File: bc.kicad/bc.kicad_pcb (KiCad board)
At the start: 2 copper layers, 90 x 50 mm, 21 parts, among them J1 Pin_Header_01x33_Male, J2 Capacitive Keyboard

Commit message: Experiment with keyboard backlighting
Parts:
- moved D5 3.88 mm to (119.3, 142.8), turned to 90 degrees
- moved D8 3.86 mm to (137.3, 142.8), turned to 90 degrees
- moved D7 3.83 mm to (131.4, 142.9), turned to 90 degrees
- moved D6 3.78 mm to (125.2, 142.8), turned to 90 degrees
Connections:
- J2 pad 1: (no net) -> /CAP_C1
- J2 pad 10: (no net) -> /CAP_A1
- J2 pad 11: (no net) -> /CAP_A#1
- J2 pad 12: (no net) -> /CAP_B1
- J2 pad 13: (no net) -> /CAP_C2
- J2 pad 2: (no net) -> /CAP_C#1
- J2 pad 3: (no net) -> /CAP_D1
- J2 pad 4: (no net) -> /CAP_D#1
- J2 pad 5: (no net) -> /CAP_E1
- J2 pad 6: (no net) -> /CAP_F1
- J2 pad 7: (no net) -> /CAP_F#1
- J2 pad 8: (no net) -> /CAP_G1
- J2 pad 9: (no net) -> /CAP_G#1
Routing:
- net /LED_GND: track 0.00 -> 176.5 mm, vias 0 -> 11
- net /LED_A1_B: track 0.00 -> 56.9 mm
- net /LED_C2_B: track 0.00 -> 54.0 mm
- net /LED_B1_B: track 0.00 -> 48.1 mm
- net /CAP_C1: track 0.00 -> 30.6 mm, vias 0 -> 1
- net /CAP_C#1: track 0.00 -> 30.1 mm, vias 0 -> 1
- net /CAP_D1: track 0.00 -> 29.3 mm, vias 0 -> 1
- net /CAP_D#1: track 0.00 -> 29.0 mm, vias 0 -> 1
- net /CAP_C2: track 0.00 -> 29.0 mm, vias 0 -> 1
- net /CAP_G1: track 0.00 -> 26.6 mm, vias 0 -> 1
- net /CAP_A1: track 0.00 -> 26.4 mm, vias 0 -> 1
- net /CAP_G#1: track 0.00 -> 26.3 mm, vias 0 -> 1
- net /CAP_F#1: track 0.00 -> 26.2 mm, vias 0 -> 1
- net /CAP_F1: track 0.00 -> 25.7 mm, vias 0 -> 1
- net /CAP_E1: track 0.00 -> 25.5 mm, vias 0 -> 1
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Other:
- board text added: "JLCJLCJLCJL"

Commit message: Layout keyboard half draft
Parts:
- removed J2: Capacitive Keyboard, bc:keyboard
- removed Ref**: Val**, bc:writing
- removed Ref**: Val**, bc:round_speaker_ring
- added BT1: CR2032, Battery:BatteryHolder_Keystone_3002_1x2032, B.Cu at (116.9, 60.6)
- added C1: 470nF, Capacitor_SMD:C_0402_1005Metric, B.Cu at (102.3, 72.1)
- added C10: 100nF, Capacitor_SMD:C_0402_1005Metric, B.Cu at (157.4, 61.5)
- added C11: 470nF, Capacitor_SMD:C_0402_1005Metric, B.Cu at (139.7, 65.6)
- added C12: 470nF, Capacitor_SMD:C_0402_1005Metric, B.Cu at (159.3, 61.6)
- added C13: 470nF, Capacitor_SMD:C_0402_1005Metric, B.Cu at (157.9, 68.9)
- added C14: 470nF, Capacitor_SMD:C_0402_1005Metric, B.Cu at (146.8, 55.5)
- added C15: 100nF, Capacitor_SMD:C_0402_1005Metric, B.Cu at (160.4, 52.3)
- added C16: 100nF, Capacitor_SMD:C_0402_1005Metric, B.Cu at (149.7, 69.3)
- added C17: 100nF, Capacitor_SMD:C_0402_1005Metric, B.Cu at (146.2, 69.5)
- added C18: 100nF, Capacitor_SMD:C_0402_1005Metric, B.Cu at (145.1, 68.0)
- added C19: 100nF, Capacitor_SMD:C_0402_1005Metric, B.Cu at (145.0, 58.4)
- added C2: 470nF, Capacitor_SMD:C_0402_1005Metric, B.Cu at (102.2, 70.8)
- added C20: 100nF, Capacitor_SMD:C_0402_1005Metric, B.Cu at (154.0, 57.3)
- added C21: Capacitive_Keyboard, bc:keyboard, F.Cu at (145.0, 75.0)
- added C3: 470nF, Capacitor_SMD:C_0402_1005Metric, B.Cu at (88.1, 73.5)
- added C4: 470nF, Capacitor_SMD:C_0402_1005Metric, B.Cu at (87.9, 75.1)
- added C5: 470nF, Capacitor_SMD:C_0402_1005Metric, B.Cu at (95.9, 67.6)
- added C6: 470nF, Capacitor_SMD:C_0402_1005Metric, B.Cu at (92.6, 67.7)
- added C7: 100nF, Capacitor_SMD:C_0402_1005Metric, B.Cu at (154.1, 68.9)
- added C8: 100nF, Capacitor_SMD:C_0402_1005Metric, B.Cu at (146.9, 56.7)
- added C9: 100nF, Capacitor_SMD:C_0402_1005Metric, B.Cu at (141.2, 65.6)
- added D17: LED_07A, bc:side_led, B.Cu at (173.7, 74.0)
- added D18: LED_03B, bc:side_led, B.Cu at (129.1, 97.0)
- added D19: LED_07B, bc:side_led, B.Cu at (171.5, 97.0)
- added D20: LED_11, bc:side_led, B.Cu at (143.4, 74.0)
- added D21: LED_04A, bc:side_led, B.Cu at (137.4, 74.0)
- added D22: LED_08A, bc:side_led, B.Cu at (181.8, 74.0)
- added D23: LED_04B, bc:side_led, B.Cu at (139.7, 97.0)
- added D24: LED_08B, bc:side_led, B.Cu at (182.0, 97.0)
- added D25: LED_12, bc:side_led, B.Cu at (155.5, 74.0)
- added D26: D_Schottky, Diode_SMD:D_SOD-123, B.Cu at (182.0, 36.0)
- added Q1: PMV48XP, Package_TO_SOT_SMD:SOT-23, B.Cu at (131.0, 55.0)
- added R1: 10K, Resistor_SMD:R_0402_1005Metric, B.Cu at (224.2, -15.0)
- added R10: 10K, Resistor_SMD:R_0402_1005Metric, B.Cu at (229.2, 20.0)
- added R11: 10K, Resistor_SMD:R_0402_1005Metric, B.Cu at (224.2, -10.0)
- added R12: 10K, Resistor_SMD:R_0402_1005Metric, B.Cu at (224.2, 19.0)
- added R13: 10K, Resistor_SMD:R_0402_1005Metric, B.Cu at (224.2, -5.00)
- added R14: 10K, Resistor_SMD:R_0402_1005Metric, B.Cu at (224.2, -20.0)
- added R15: 10K, Resistor_SMD:R_0402_1005Metric, B.Cu at (228.8, 1.00)
- added R16: 10K, Resistor_SMD:R_0402_1005Metric, B.Cu at (223.8, 1.00)
- added R2: 10K, Resistor_SMD:R_0402_1005Metric, B.Cu at (229.2, -5.00)
- added R3: 10K, Resistor_SMD:R_0402_1005Metric, B.Cu at (142.6, 52.6)
- added R4: 10K, Resistor_SMD:R_0402_1005Metric, B.Cu at (224.0, 26.0)
- added R5: 10K, Resistor_SMD:R_0402_1005Metric, B.Cu at (224.2, 13.0)
- added R6: 10K, Resistor_SMD:R_0402_1005Metric, B.Cu at (224.2, 7.00)
- added R7: 10K, Resistor_SMD:R_0402_1005Metric, B.Cu at (229.2, -11.0)
- added R8: 10K, Resistor_SMD:R_0402_1005Metric, B.Cu at (228.2, 13.0)
- added R9: 10K, Resistor_SMD:R_0402_1005Metric, B.Cu at (228.8, 7.00)
- added SW1: SW_Push, bc:SW_Push_1P1T_NO_5.1x5.1mm_H2.5mm, B.Cu at (167.1, 63.4)
- added TP1: Catch, bc:test_point, B.Cu at (102.0, 53.0)
- added TP2: Catch, bc:test_point, B.Cu at (102.0, 97.1)
- added TP3: Catch, bc:test_point, B.Cu at (135.7, 68.0)
- added TP4: Catch, bc:test_point, B.Cu at (188.0, 53.0)
- added TP5: Catch, bc:test_point, B.Cu at (188.0, 97.1)
- added U1: STM32L052C8Tx, Package_QFP:LQFP-48_7x7mm_P0.5mm, B.Cu at (149.7, 63.2)
- D1: value LED_C1 -> D_Schottky; footprint bc:side_led -> Diode_SMD:D_SOD-123
- D10: value LED_A1_T -> LED_13
- D11: value LED_A1_B -> LED_02A
- D12: value LED_A#1 -> LED_06A
- D13: value LED_B1_T -> LED_02B
- D14: value LED_B1_B -> LED_06B
- D15: value LED_C2_T -> LED_10
- D16: value LED_C2_B -> LED_03A
- D2: value LED_C#1 -> D_Schottky; footprint bc:side_led -> Diode_SMD:D_SOD-123
- D3: value LED_D1 -> D_Schottky; footprint bc:side_led -> Diode_SMD:D_SOD-123
- D4: value LED_D#1 -> D_Schottky; footprint bc:side_led -> Diode_SMD:D_SOD-123
- D5: value LED_E1 -> LED_01A
- D6: value LED_F1 -> LED_05A
- D7: value LED_F#1 -> LED_01B
- D8: value LED_G1 -> LED_05B
- D9: value LED_G#1 -> LED_09
- J1: value Pin_Header_01x33_Male -> Edge Connector; footprint Connector_PinHeader_2.54mm:PinHeader_1x33_P2.54mm_Vertical_SMD_Pin1Left -> bc:edge_connector
- LS1: value Speaker -> Transducer; footprint bc:wire_pad_3x5mm_x2 -> bc:transducer
- moved D1 148.4 mm to (202.3, 41.0), turned to 0 degrees
- moved D3 138.5 mm to (188.4, 30.0), turned to 0 degrees
- moved D4 138.3 mm to (199.3, 34.0), turned to 0 degrees
- moved D2 136.8 mm to (191.3, 40.0), turned to 0 degrees
- moved LS1 110.1 mm to (177.9, 63.2), turned to 180 degrees
- moved D16 98.7 mm to (131.1, 74.0), turned to 180 degrees
- moved D11 95.8 mm to (118.4, 74.0), turned to 180 degrees
- moved D15 79.7 mm to (124.8, 74.0)
- moved J1 75.7 mm to (163.0, 51.9), turned to 0 degrees
- moved D9 73.2 mm to (112.1, 74.0)
- moved D6 72.9 mm to (149.5, 74.0), turned to 180 degrees
- moved D5 70.2 mm to (105.9, 74.0), turned to 180 degrees
- moved D10 69.9 mm to (167.6, 74.0)
- moved D14 68.5 mm to (160.9, 97.0)
- moved D12 67.5 mm to (161.5, 74.0)
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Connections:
- D1 pad 1: /LED_GND -> Net-(C1-Pad2)
- D1 pad 2: /LED_C1 -> /LED_R0_PWR
- D10 pad 1: /LED_GND -> /LED_C0
- D10 pad 2: /LED_A1_T -> Net-(C6-Pad2)
- D11 pad 1: /LED_GND -> /LED_C1
- D11 pad 2: /LED_A1_B -> Net-(C1-Pad2)
- D12 pad 1: /LED_GND -> /LED_C1
- D12 pad 2: /LED_A#1 -> Net-(C3-Pad2)
- D13 pad 1: /LED_GND -> /LED_C1
- D13 pad 2: /LED_B1_T -> Net-(C1-Pad2)
- D14 pad 1: /LED_GND -> /LED_C1
- D14 pad 2: /LED_B1_B -> Net-(C3-Pad2)
- D15 pad 1: /LED_GND -> /LED_C1
- D15 pad 2: /LED_C2_T -> Net-(C5-Pad2)
- D16 pad 1: /LED_GND -> /LED_C2
- D16 pad 2: /LED_C2_B -> Net-(C1-Pad2)
- D2 pad 1: /LED_GND -> Net-(C3-Pad2)
- D2 pad 2: /LED_C#1 -> /LED_R1_PWR
- D3 pad 1: /LED_GND -> Net-(C5-Pad2)
- D3 pad 2: /LED_D1 -> /LED_R2_PWR
- D4 pad 1: /LED_GND -> Net-(C6-Pad2)
- D4 pad 2: /LED_D#1 -> /LED_R3_PWR
- D5 pad 1: /LED_GND -> /LED_C0
- D5 pad 2: /LED_E1 -> Net-(C1-Pad2)
- D6 pad 1: /LED_GND -> /LED_C0
- D6 pad 2: /LED_F1 -> Net-(C3-Pad2)
- D7 pad 1: /LED_GND -> /LED_C0
- D7 pad 2: /LED_F#1 -> Net-(C1-Pad2)
- D8 pad 1: /LED_GND -> /LED_C0
- D8 pad 2: /LED_G1 -> Net-(C3-Pad2)
- D9 pad 1: /LED_GND -> /LED_C0
- D9 pad 2: /LED_G#1 -> Net-(C5-Pad2)
- J1 pad 1: /SPEAKER+ -> GND
- J1 pad 2: /SPEAKER- -> /NRST
- J1 pad 3: /CAP_C1 -> /SWCLK
- J1 pad 4: /LED_C1 -> /SWDIO
- J1 pad 5: /CAP_C#1 -> /KEY_03_D1
- J1 pad 6: /LED_C#1 -> /KEY_02_C#1
- J1 pad 7: /CAP_D1 -> /BOOT0
- J1 pad 8: /LED_D1 -> VDD
- LS1 pad 1: /SPEAKER+ -> /TRANSDUCER
- LS1 pad 2: /SPEAKER- -> GND
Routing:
- net /LED_GND: track 176.5 -> 0.00 mm, vias 11 -> 0
- net Net-(C3-Pad2): track 0.00 -> 146.3 mm
- net Net-(C1-Pad2): track 0.00 -> 144.6 mm
- net /LED_C0: track 0.00 -> 70.3 mm
- net /LED_C3: track 0.00 -> 67.7 mm
- net /LED_C2: track 0.00 -> 57.6 mm
- net /LED_A1_B: track 56.9 -> 0.00 mm
- net /LED_C2_B: track 54.0 -> 0.00 mm
- net /LED_B1_B: track 48.1 -> 0.00 mm
- net /LED_C1: track 22.0 -> 67.3 mm
- net /CAP_C1: track 30.6 -> 0.00 mm, vias 1 -> 0
- net /CAP_C#1: track 30.1 -> 0.00 mm, vias 1 -> 0
- net /CAP_D1: track 29.3 -> 0.00 mm, vias 1 -> 0
- net /CAP_D#1: track 29.0 -> 0.00 mm, vias 1 -> 0
- net /CAP_C2: track 29.0 -> 0.00 mm, vias 1 -> 0
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- added copper zone on B.Cu, net GND
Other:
- outline, holes or cut-outs redrawn
- rule trace_min: 0.2 -> 0.15
- rule via_min_drill: 0.3 -> 0.2
- rule via_min_size: 0.4 -> 0.45
- board text removed: "JLCJLCJLCJL"

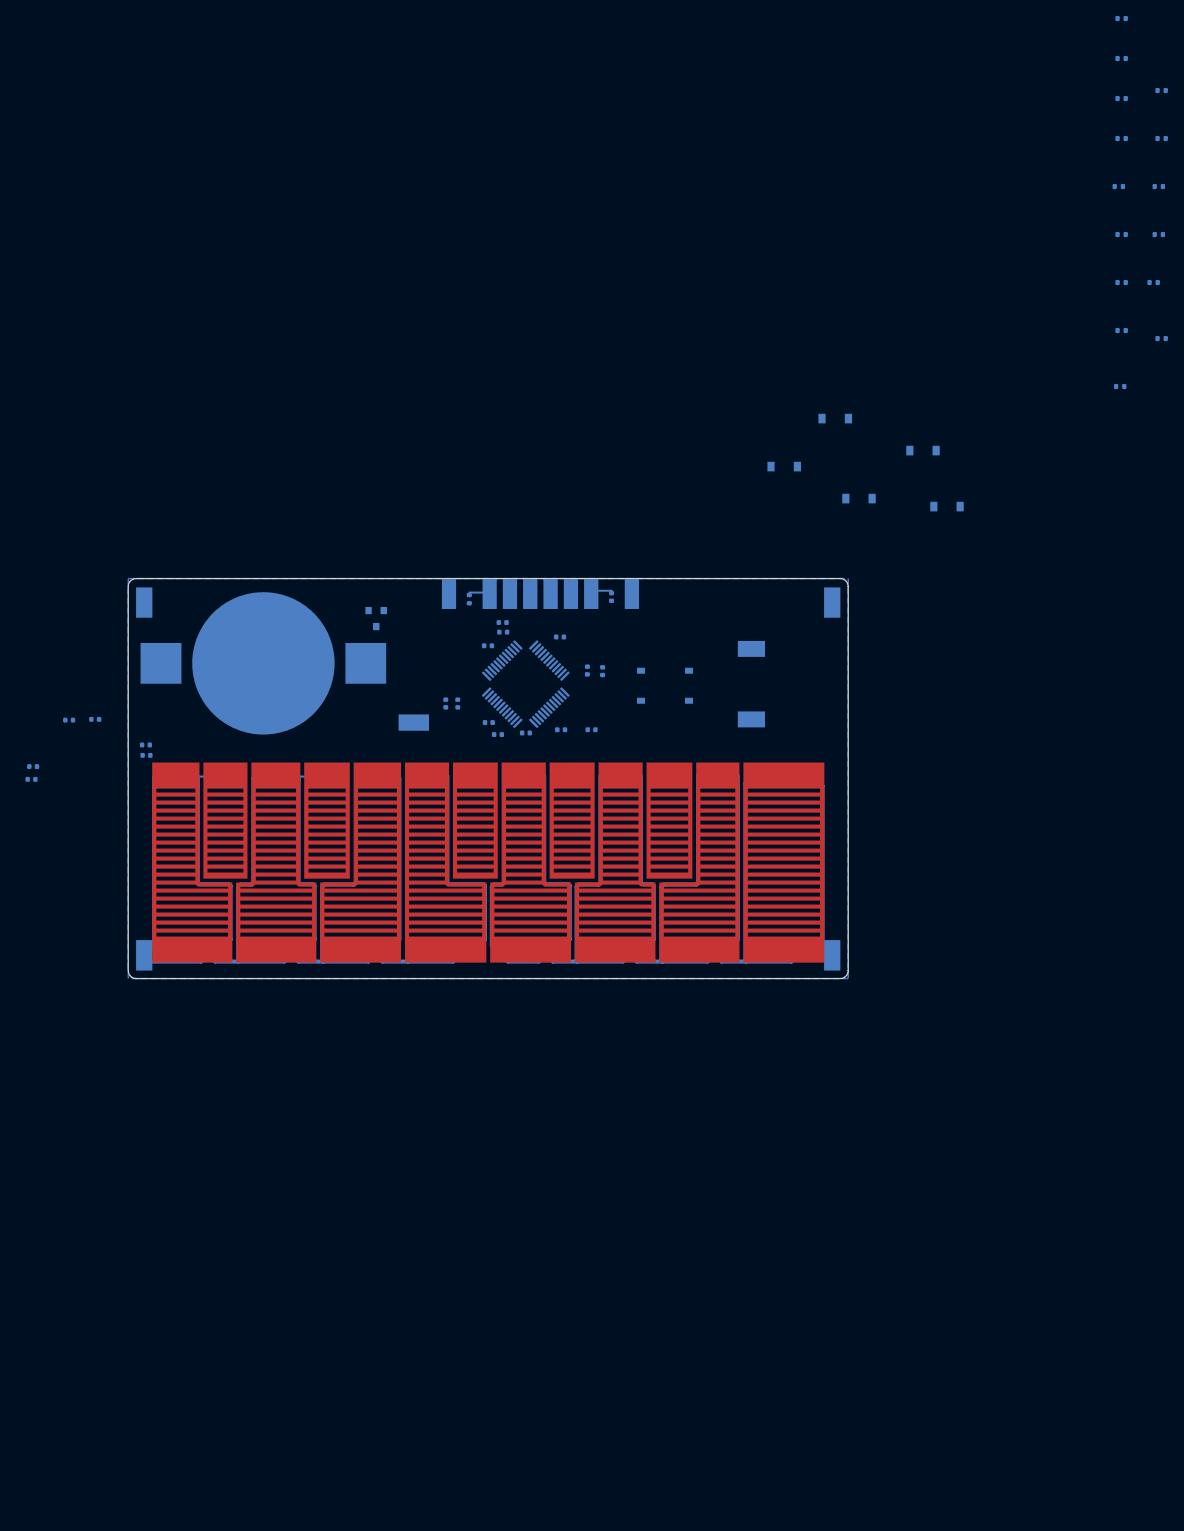
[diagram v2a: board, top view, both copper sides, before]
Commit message: Block as much light as possible between keys
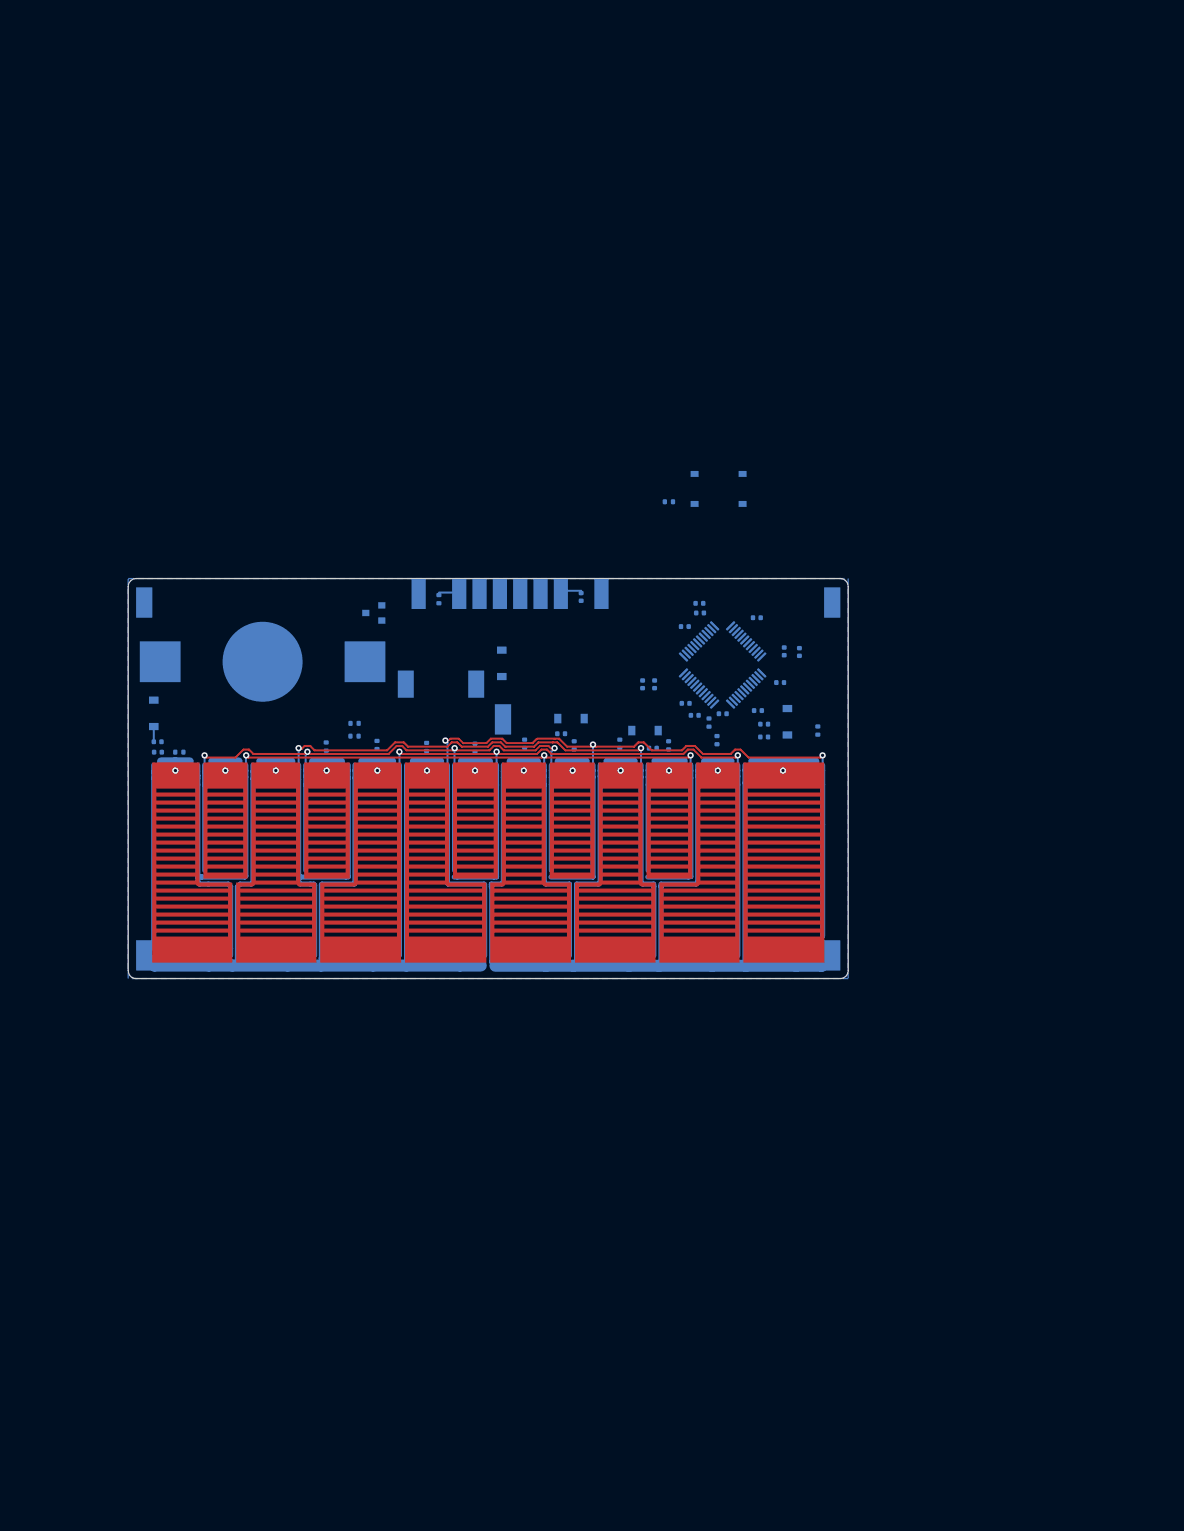
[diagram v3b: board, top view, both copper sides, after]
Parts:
- BT1: footprint Battery:BatteryHolder_Keystone_3002_1x2032 -> bc:BatteryHolder_Keystone_3002_1x2032
- moved R16 137.1 mm to (106.4, 71.7), turned to 180 degrees
- moved R14 131.3 mm to (128.3, 69.7), turned to 180 degrees
- moved R13 125.1 mm to (124.8, 71.0), turned to 270 degrees
- moved R15 120.9 mm to (128.3, 68.1), turned to 180 degrees
- moved R11 118.8 mm to (137.3, 71.0), turned to 270 degrees
- moved R12 106.5 mm to (131.1, 70.8), turned to 270 degrees
- moved R7 106.1 mm to (161.4, 70.7), turned to 270 degrees
- moved D1 102.5 mm to (103.2, 66.8), turned to 90 degrees
- moved R9 101.7 mm to (149.6, 70.7), turned to 270 degrees
- moved R10 99.9 mm to (143.3, 71.2), turned to 270 degrees
- moved R8 92.7 mm to (155.8, 70.8), turned to 270 degrees
- moved R2 92.4 mm to (172.6, 68.0), turned to 90 degrees
- moved C4 91.7 mm to (179.5, 69.8)
- moved C3 91.5 mm to (179.5, 68.2)
- moved R6 85.3 mm to (167.6, 70.8), turned to 270 degrees
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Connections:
- TP5 pad 1: /LED_C3 -> Net-(C3-Pad2)
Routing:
- net Net-(C5-Pad2): track 0.00 -> 110.0 mm, vias 0 -> 4
- net /LED_C0: track 70.3 -> 170.5 mm, vias 0 -> 3
- net /LED_C3: track 67.7 -> 146.9 mm, vias 0 -> 3
- net /LED_C2: track 57.6 -> 131.9 mm, vias 0 -> 3
- net /LED_C1: track 67.3 -> 137.6 mm, vias 0 -> 2
- net Net-(C3-Pad2): track 146.3 -> 163.3 mm
- net Net-(C1-Pad2): track 144.6 -> 160.9 mm
- net Net-(C6-Pad2): track 0.00 -> 14.0 mm
- net Net-(C21-Pad13): track 0.00 -> 9.05 mm, vias 0 -> 1
- net Net-(C21-Pad3): track 0.00 -> 5.05 mm, vias 0 -> 1
- net Net-(C21-Pad5): track 0.00 -> 4.90 mm, vias 0 -> 1
- net Net-(C21-Pad1): track 0.00 -> 4.75 mm, vias 0 -> 1
- net Net-(C21-Pad11): track 0.00 -> 4.75 mm, vias 0 -> 1
- net Net-(C21-Pad4): track 0.00 -> 4.65 mm, vias 0 -> 1
- net Net-(C21-Pad7): track 0.00 -> 4.55 mm, vias 0 -> 1
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
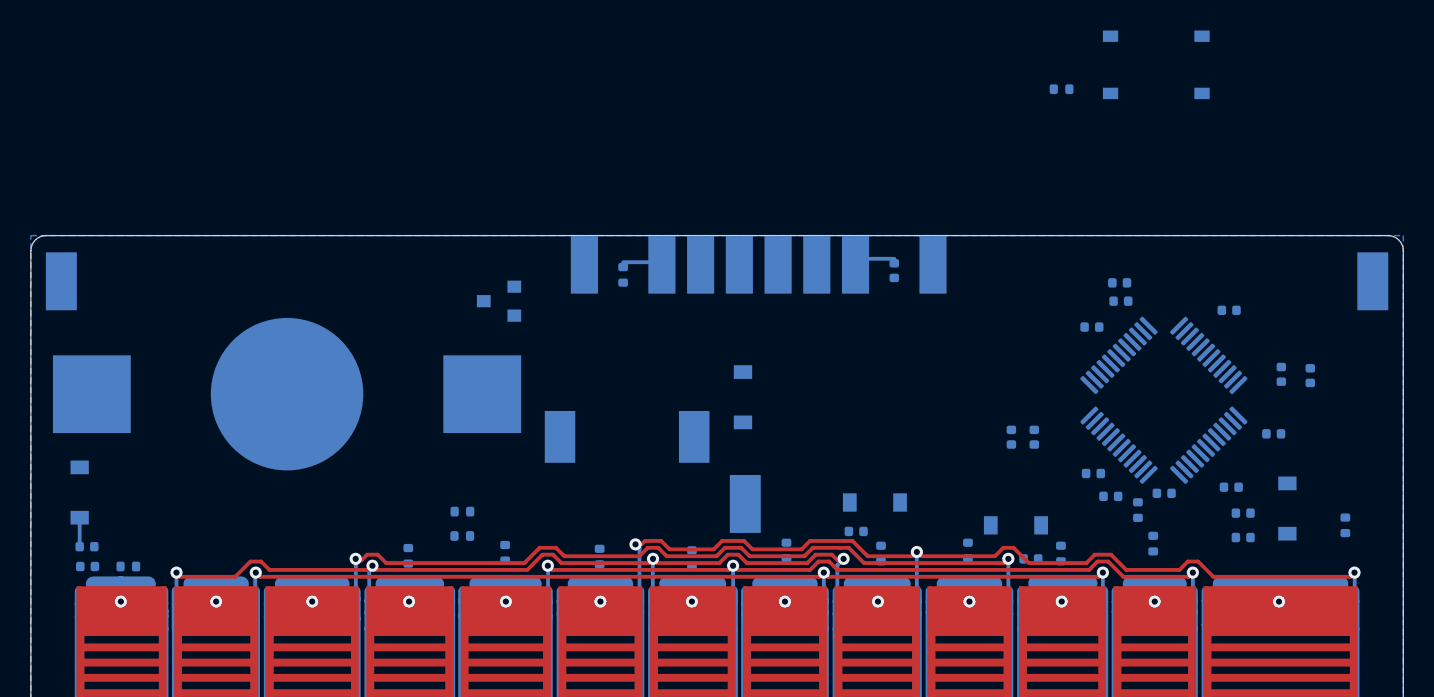
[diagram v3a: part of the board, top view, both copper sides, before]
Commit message: Attempt pasta plate routing on the front
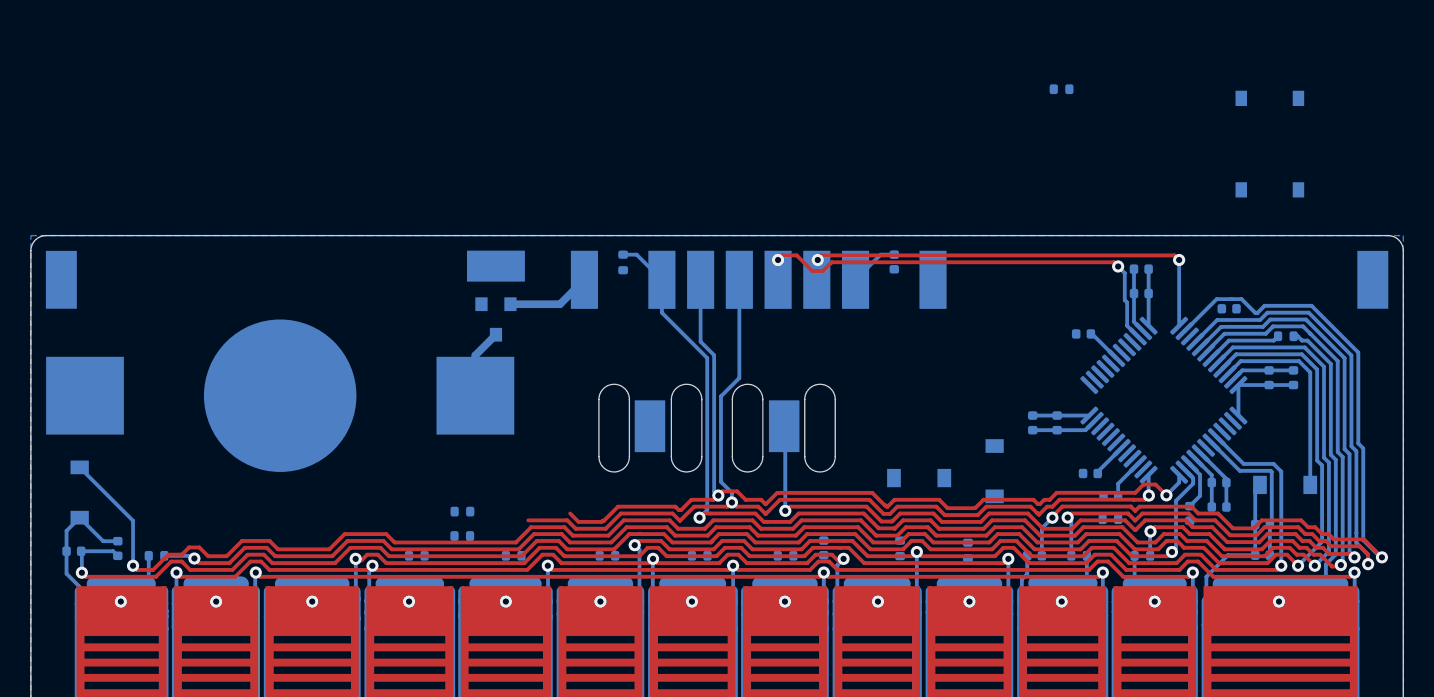
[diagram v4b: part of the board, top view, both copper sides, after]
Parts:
- removed D26: D_Schottky, Diode_SMD:D_SOD-123
- moved TP3 22.6 mm to (130.5, 52.0), turned to 0 degrees
- moved R4 13.0 mm to (182.3, 56.6), turned to 0 degrees
- moved SW1 9.09 mm to (181.2, 44.0), turned to 90 degrees
- moved C13 5.99 mm to (177.9, 67.8)
- moved LS1 5.94 mm to (145.0, 62.5)
- moved D4 3.82 mm to (163.2, 65.5), turned to 90 degrees
- moved D3 3.31 mm to (158.2, 65.9)
- moved C3 3.04 mm to (180.8, 71.0), turned to 180 degrees
- moved C5 2.38 mm to (152.0, 70.5), turned to 270 degrees
- moved C16 2.14 mm to (176.0, 68.2), turned to 90 degrees
- moved C2 2.02 mm to (105.7, 70.5), turned to 90 degrees
- moved R16 1.98 mm to (108.2, 71.0)
- moved R2 1.91 mm to (170.8, 68.6), turned to 0 degrees
- moved C9 1.77 mm to (167.3, 62.3)
- moved C11 1.69 mm to (165.7, 62.3)
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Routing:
- net /LED_R0_PWR: track 0.00 -> 112.7 mm, vias 0 -> 2
- net /LED_R0_CLK: track 0.00 -> 100.9 mm, vias 0 -> 2
- net /BOOT0: track 2.60 -> 86.4 mm, vias 0 -> 2
- net /KEY_01_C1: track 0.00 -> 78.0 mm, vias 0 -> 2
- net /TRANSDUCER: track 0.00 -> 71.3 mm, vias 0 -> 2
- net /KEY_03_D1: track 0.00 -> 61.3 mm, vias 0 -> 2
- net /KEY_02_C#1: track 0.00 -> 59.3 mm, vias 0 -> 2
- net /LED_R3_CLK: track 0.00 -> 55.0 mm, vias 0 -> 2
- net /KEY_11_A#1: track 0.00 -> 51.3 mm, vias 0 -> 2
- net /KEY_12_B1: track 0.00 -> 39.6 mm, vias 0 -> 2
- net /SWDIO: track 0.00 -> 28.3 mm, vias 0 -> 2
- net /SWCLK: track 0.00 -> 28.3 mm, vias 0 -> 2
- net VDD: track 0.00 -> 22.2 mm
- net Net-(C21-Pad13): track 9.05 -> 27.2 mm
- net GND: track 0.00 -> 17.1 mm
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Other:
- outline, holes or cut-outs redrawn
